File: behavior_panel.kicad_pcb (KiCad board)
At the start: 2 copper layers, 22 x 60 mm, 32 parts, among them J1 Conn_01x16, Q1 Q_NPN_BEC, Q3 N-channel MOSFET, U1 LM2902, U2 LM317_3PinPackage, U3 SFH617A-1X007T

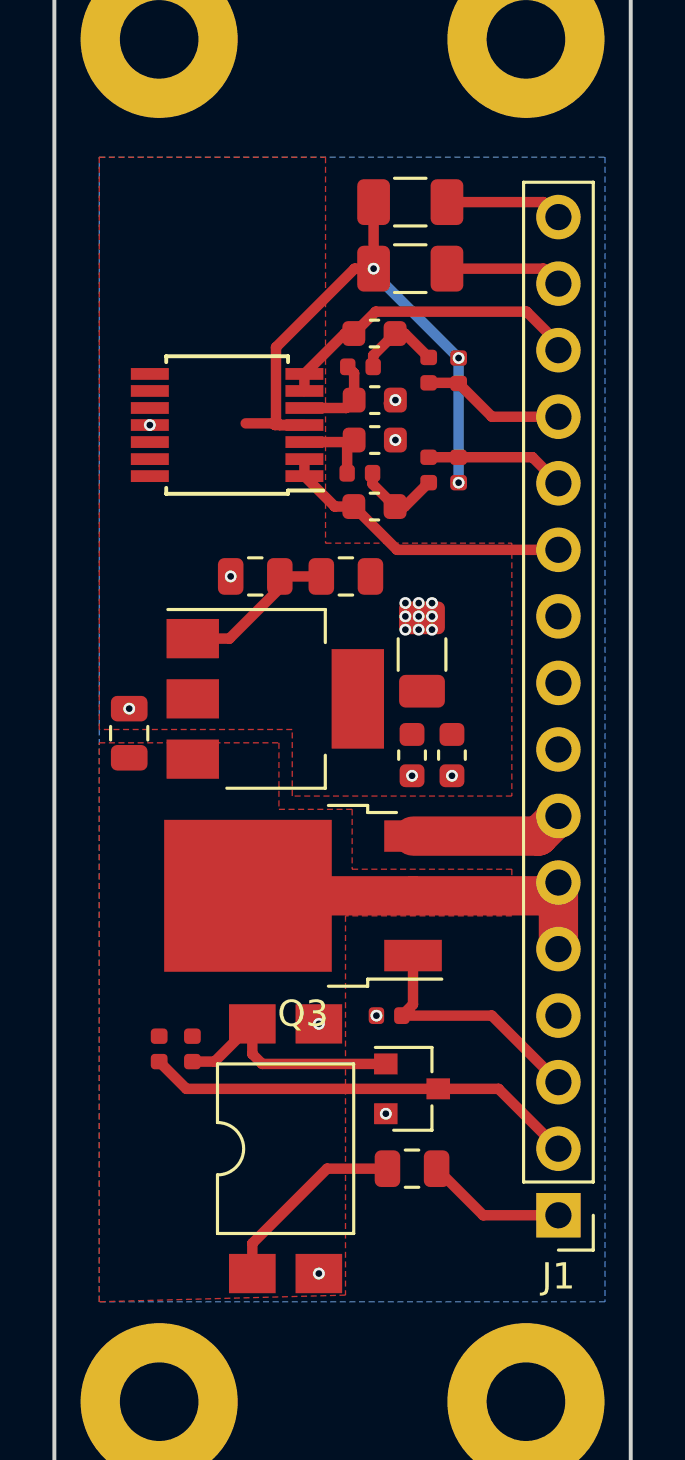
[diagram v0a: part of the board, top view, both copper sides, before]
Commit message: Fix bug in MOSFET light control
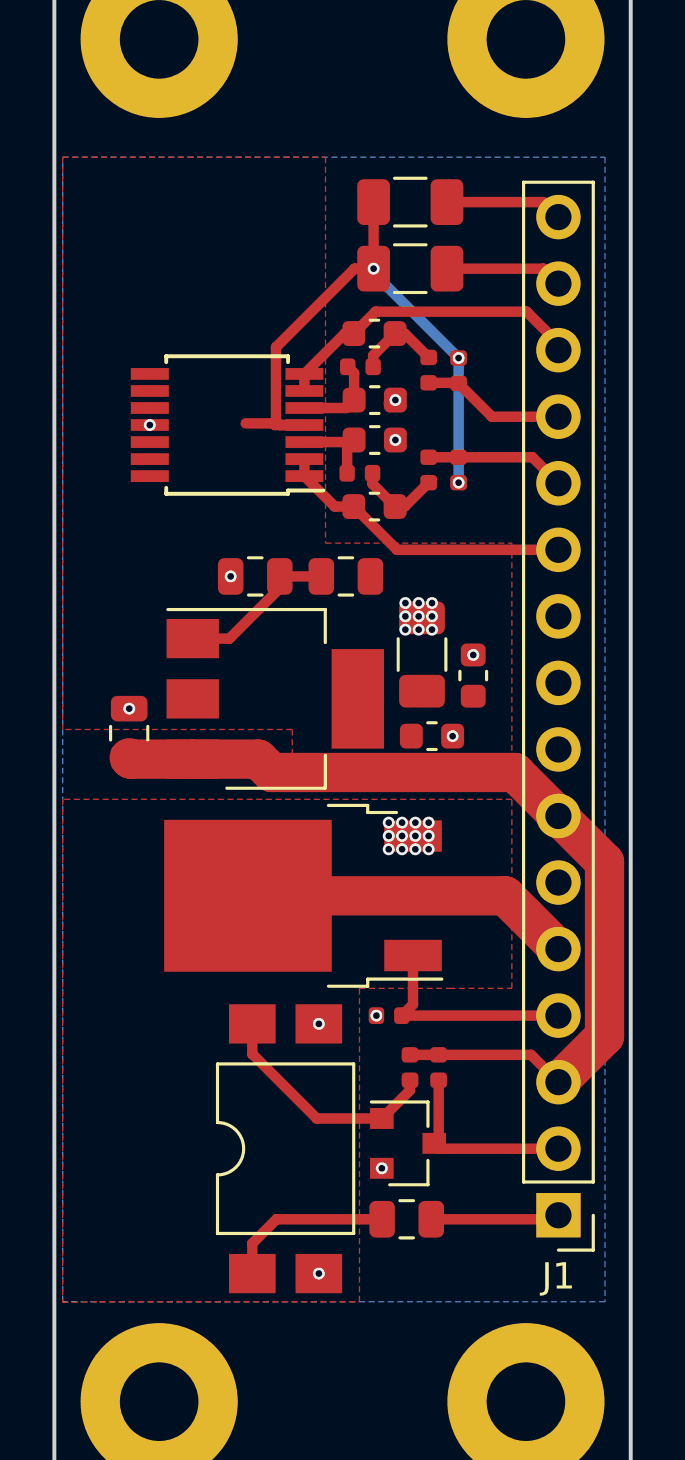
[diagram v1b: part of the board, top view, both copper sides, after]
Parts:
- moved R9 10.7 mm to (137.7, 82.2)
- moved R19 8.34 mm to (136.6, 82.2)
- moved C12 3.14 mm to (139.0, 67.3), turned to 90 degrees
- moved Q1 2.09 mm to (136.5, 85.1)
- moved R10 1.94 mm to (136.4, 88.0)
- moved C6 1.05 mm to (137.4, 69.6), turned to 180 degrees
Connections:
- net PD_IN renamed PD_CTL
- J1 pad 3: LT_IN -> +28V
- J1 pad 4: GND -> LT_CTL
- J1 pad 5: +28V -> LT_IN
- J1 pad 6: +28V -> GND
- J1 pad 7: LT_OUT -> +28V
- Q3 pad 1: LT_IN -> LT_CTL
- Q3 pad 2: +28V -> LT_IN
- Q3 pad 3: LT_OUT -> GND
- R25 pad 1: LT_IN -> LT_CTL
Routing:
- net +28V: track 14.6 -> 35.0 mm
- net PD_OUT: track 16.6 -> 7.30 mm
- net LT_CTL: track 0.00 -> 8.45 mm
- net LT_OUT: track 5.87 -> 0.00 mm
- net LT_IN: track 9.50 -> 12.7 mm
- net Net-(R10-Pad2): track 7.49 -> 6.49 mm
- net GND: vias 20 -> 32
- added copper zone on F.Cu, net LT_IN
- removed copper zone on F.Cu, net +28V
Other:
- board text added: "FROM LT"
- board text removed: "TO LT"

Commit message: Update to Kicad 6
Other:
- net class Default removed
- rule pad_to_mask_clearance: 0.2 -> 0

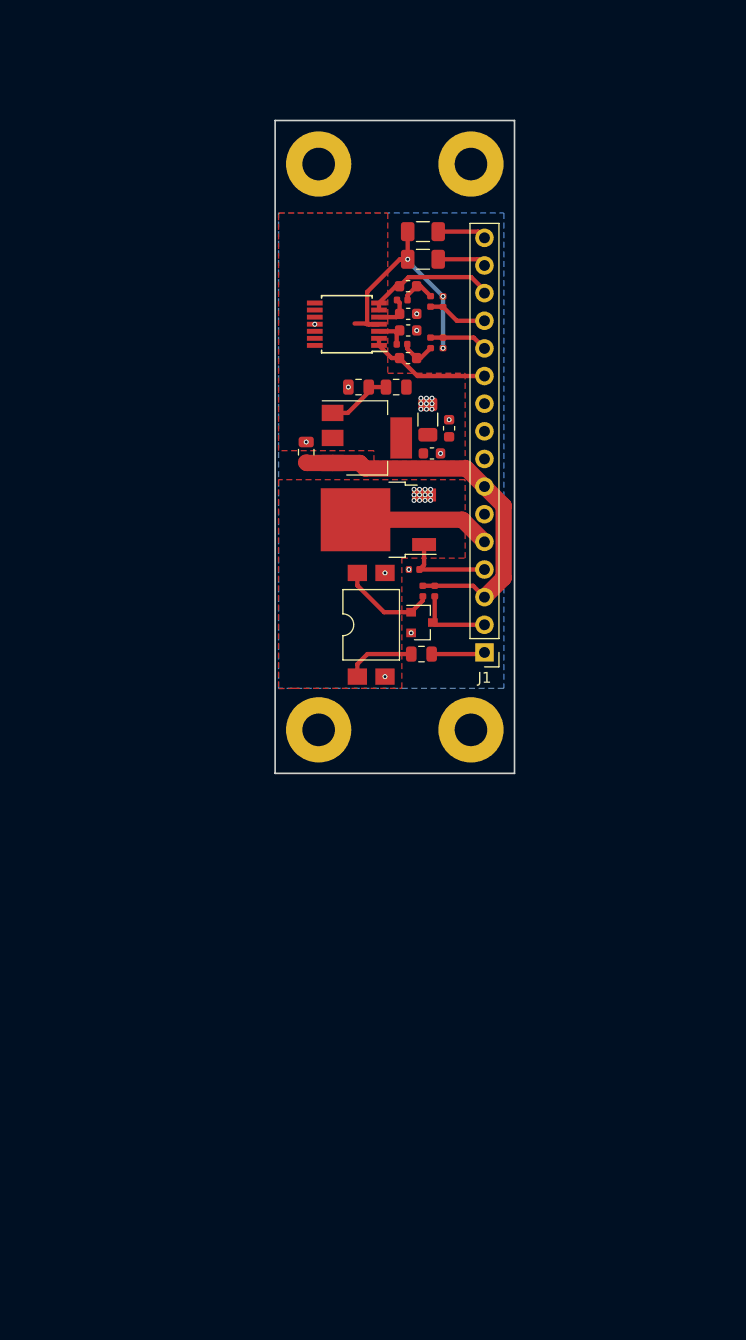
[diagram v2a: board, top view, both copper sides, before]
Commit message: Updated to include four power relays and four IR circuts
Went back to the through-hole, hand-solderable version.
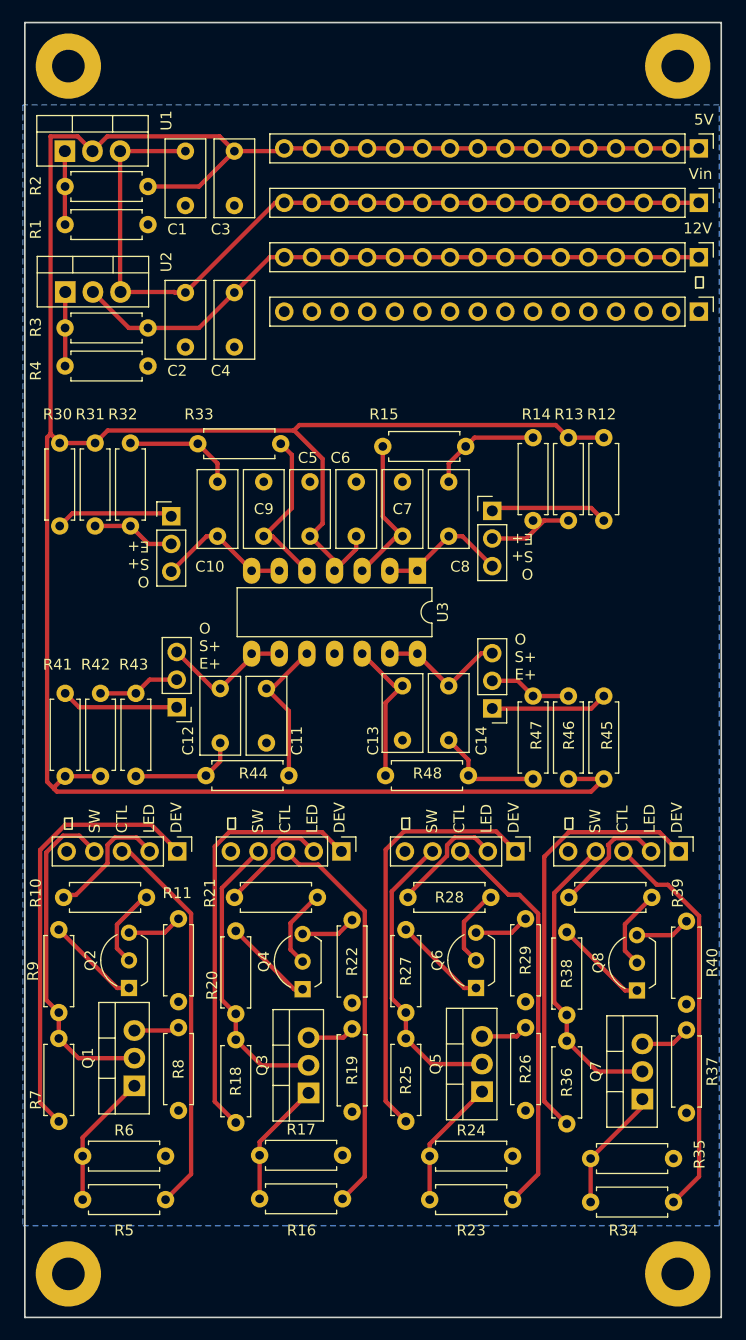
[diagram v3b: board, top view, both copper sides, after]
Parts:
- added C10: 0.1uF, Capacitor_THT:C_Rect_L7.0mm_W3.5mm_P5.00mm, F.Cu at (117.7, 77.2)
- added C13: 0.1uF, Capacitor_THT:C_Rect_L7.0mm_W3.5mm_P5.00mm, F.Cu at (134.7, 91.0)
- added C14: 0.1uF, Capacitor_THT:C_Rect_L7.0mm_W3.5mm_P5.00mm, F.Cu at (139.0, 91.0)
- added C7: 0.1uF, Capacitor_THT:C_Rect_L7.0mm_W3.5mm_P5.00mm, F.Cu at (134.7, 77.2)
- added C8: 0.1uF, Capacitor_THT:C_Rect_L7.0mm_W3.5mm_P5.00mm, F.Cu at (139.0, 77.2)
- added C9: 0.1uF, Capacitor_THT:C_Rect_L7.0mm_W3.5mm_P5.00mm, F.Cu at (122.0, 77.2)
- added J17: Conn_01x05_Pin, Connector_PinHeader_2.54mm:PinHeader_1x05_P2.54mm_Vertical, F.Cu at (114.0, 106.2)
- added J18: Conn_01x03_Pin, Connector_PinHeader_2.54mm:PinHeader_1x03_P2.54mm_Vertical, F.Cu at (143.0, 74.9)
- added J19: Conn_01x05_Pin, Connector_PinHeader_2.54mm:PinHeader_1x05_P2.54mm_Vertical, F.Cu at (129.1, 106.2)
- added J2: Conn_01x16, Connector_PinHeader_2.54mm:PinHeader_1x16_P2.54mm_Vertical, F.Cu at (161.9, 51.6)
- added J20: Conn_01x05_Pin, Connector_PinHeader_2.54mm:PinHeader_1x05_P2.54mm_Vertical, F.Cu at (145.1, 106.2)
- added J21: Conn_01x03_Pin, Connector_PinHeader_2.54mm:PinHeader_1x03_P2.54mm_Vertical, F.Cu at (113.5, 75.4)
- added J22: Conn_01x05_Pin, Connector_PinHeader_2.54mm:PinHeader_1x05_P2.54mm_Vertical, F.Cu at (160.1, 106.2)
- added J23: Conn_01x03_Pin, Connector_PinHeader_2.54mm:PinHeader_1x03_P2.54mm_Vertical, F.Cu at (114.0, 92.9)
- added J24: Conn_01x03_Pin, Connector_PinHeader_2.54mm:PinHeader_1x03_P2.54mm_Vertical, F.Cu at (143.0, 93.0)
- added J3: Conn_01x16, Connector_PinHeader_2.54mm:PinHeader_1x16_P2.54mm_Vertical, F.Cu at (161.9, 46.6)
- added J4: Conn_01x16, Connector_PinHeader_2.54mm:PinHeader_1x16_P2.54mm_Vertical, F.Cu at (161.9, 56.6)
- added Q2: Q_NPN_BCE, Package_TO_SOT_THT:TO-92L_Inline_Wide, F.Cu at (109.6, 118.7)
- added Q4: Q_NPN_BCE, Package_TO_SOT_THT:TO-92L_Inline_Wide, F.Cu at (125.5, 118.8)
- added Q5: N MOSFET, Package_TO_SOT_THT:TO-220-3_Vertical, F.Cu at (142.0, 128.3)
- added Q6: Q_NPN_BCE, Package_TO_SOT_THT:TO-92L_Inline_Wide, F.Cu at (141.5, 118.7)
- added Q7: N MOSFET, Package_TO_SOT_THT:TO-220-3_Vertical, F.Cu at (156.8, 128.9)
- added Q8: Q_NPN_BCE, Package_TO_SOT_THT:TO-92L_Inline_Wide, F.Cu at (156.3, 119.0)
- added R11: 10k, Resistor_THT:R_Axial_DIN0207_L6.3mm_D2.5mm_P7.62mm_Horizontal, F.Cu at (114.1, 112.4)
- added R12: 100 0.25W, Resistor_THT:R_Axial_DIN0207_L6.3mm_D2.5mm_P7.62mm_Horizontal, F.Cu at (153.2, 68.1)
- added R13: 10k, Resistor_THT:R_Axial_DIN0207_L6.3mm_D2.5mm_P7.62mm_Horizontal, F.Cu at (150.0, 68.1)
- added R14: 10k, Resistor_THT:R_Axial_DIN0207_L6.3mm_D2.5mm_P7.62mm_Horizontal, F.Cu at (146.7, 68.1)
- added R15: 10k, Resistor_THT:R_Axial_DIN0207_L6.3mm_D2.5mm_P7.62mm_Horizontal, F.Cu at (132.9, 69.0)
- added R16: 2.2k, Resistor_THT:R_Axial_DIN0207_L6.3mm_D2.5mm_P7.62mm_Horizontal, F.Cu at (129.2, 138.1)
- added R20: 10k, Resistor_THT:R_Axial_DIN0207_L6.3mm_D2.5mm_P7.62mm_Horizontal, F.Cu at (119.4, 121.1)
- added R21: 10k, Resistor_THT:R_Axial_DIN0207_L6.3mm_D2.5mm_P7.62mm_Horizontal, F.Cu at (119.3, 110.4)
- added R22: 10k, Resistor_THT:R_Axial_DIN0207_L6.3mm_D2.5mm_P7.62mm_Horizontal, F.Cu at (130.1, 112.5)
- added R23: 2.2k, Resistor_THT:R_Axial_DIN0207_L6.3mm_D2.5mm_P7.62mm_Horizontal, F.Cu at (144.8, 138.2)
- added R24: 10k, Resistor_THT:R_Axial_DIN0207_L6.3mm_D2.5mm_P7.62mm_Horizontal, F.Cu at (137.2, 134.2)
- added R26: R, Resistor_THT:R_Axial_DIN0207_L6.3mm_D2.5mm_P7.62mm_Horizontal, F.Cu at (146.0, 122.4)
- added R27: 10k, Resistor_THT:R_Axial_DIN0207_L6.3mm_D2.5mm_P7.62mm_Horizontal, F.Cu at (135.0, 121.0)
- added R28: 10k, Resistor_THT:R_Axial_DIN0207_L6.3mm_D2.5mm_P7.62mm_Horizontal, F.Cu at (135.2, 110.4)
- added R29: 10k, Resistor_THT:R_Axial_DIN0207_L6.3mm_D2.5mm_P7.62mm_Horizontal, F.Cu at (146.0, 112.4)
- added R30: 100 0.25W, Resistor_THT:R_Axial_DIN0207_L6.3mm_D2.5mm_P7.62mm_Horizontal, F.Cu at (103.2, 68.6)
- added R31: 10k, Resistor_THT:R_Axial_DIN0207_L6.3mm_D2.5mm_P7.62mm_Horizontal, F.Cu at (106.5, 68.6)
- added R32: 10k, Resistor_THT:R_Axial_DIN0207_L6.3mm_D2.5mm_P7.62mm_Horizontal, F.Cu at (109.7, 68.6)
- added R33: 10k, Resistor_THT:R_Axial_DIN0207_L6.3mm_D2.5mm_P7.62mm_Horizontal, F.Cu at (123.5, 68.7)
- added R34: 2.2k, Resistor_THT:R_Axial_DIN0207_L6.3mm_D2.5mm_P7.62mm_Horizontal, F.Cu at (159.6, 138.4)
- added R35: 10k, Resistor_THT:R_Axial_DIN0207_L6.3mm_D2.5mm_P7.62mm_Horizontal, F.Cu at (152.0, 134.4)
- added R36: 50, Resistor_THT:R_Axial_DIN0207_L6.3mm_D2.5mm_P7.62mm_Horizontal, F.Cu at (149.8, 123.6)
- added R37: R, Resistor_THT:R_Axial_DIN0207_L6.3mm_D2.5mm_P7.62mm_Horizontal, F.Cu at (160.8, 122.6)
- added R38: 10k, Resistor_THT:R_Axial_DIN0207_L6.3mm_D2.5mm_P7.62mm_Horizontal, F.Cu at (149.8, 121.2)
- added R39: 10k, Resistor_THT:R_Axial_DIN0207_L6.3mm_D2.5mm_P7.62mm_Horizontal, F.Cu at (150.0, 110.4)
- added R40: 10k, Resistor_THT:R_Axial_DIN0207_L6.3mm_D2.5mm_P7.62mm_Horizontal, F.Cu at (160.8, 112.6)
- added R41: 100 0.25W, Resistor_THT:R_Axial_DIN0207_L6.3mm_D2.5mm_P7.62mm_Horizontal, F.Cu at (103.7, 99.3)
- added R42: 10k, Resistor_THT:R_Axial_DIN0207_L6.3mm_D2.5mm_P7.62mm_Horizontal, F.Cu at (107.0, 99.3)
- added R43: 10k, Resistor_THT:R_Axial_DIN0207_L6.3mm_D2.5mm_P7.62mm_Horizontal, F.Cu at (110.2, 99.3)
- added R44: 10k, Resistor_THT:R_Axial_DIN0207_L6.3mm_D2.5mm_P7.62mm_Horizontal, F.Cu at (124.3, 99.2)
- added R45: 100 0.25W, Resistor_THT:R_Axial_DIN0207_L6.3mm_D2.5mm_P7.62mm_Horizontal, F.Cu at (153.2, 99.5)
- added R46: 10k, Resistor_THT:R_Axial_DIN0207_L6.3mm_D2.5mm_P7.62mm_Horizontal, F.Cu at (150.0, 99.5)
- added R47: 10k, Resistor_THT:R_Axial_DIN0207_L6.3mm_D2.5mm_P7.62mm_Horizontal, F.Cu at (146.7, 99.5)
- added R48: 10k, Resistor_THT:R_Axial_DIN0207_L6.3mm_D2.5mm_P7.62mm_Horizontal, F.Cu at (133.1, 99.2)
- C1, C2, C6: footprint Capacitor_SMD:C_0603_1608Metric -> Capacitor_THT:C_Rect_L7.0mm_W3.5mm_P5.00mm
- C11: footprint Capacitor_SMD:C_0805_2012Metric -> Capacitor_THT:C_Rect_L7.0mm_W3.5mm_P5.00mm
- C12: value 1uF -> 0.1uF; footprint Capacitor_SMD:C_0603_1608Metric -> Capacitor_THT:C_Rect_L7.0mm_W3.5mm_P5.00mm
- C3, C4: value 0.1uF -> 1uF; footprint Capacitor_SMD:C_0603_1608Metric -> Capacitor_THT:C_Rect_L7.0mm_W3.5mm_P5.00mm
- C5: footprint Capacitor_SMD:C_1206_3216Metric -> Capacitor_THT:C_Rect_L7.0mm_W3.5mm_P5.00mm
- Q1: value Q_NPN_BEC -> N MOSFET; footprint Package_TO_SOT_SMD:SOT-23 -> Package_TO_SOT_THT:TO-220-3_Vertical
- Q3: value N-channel MOSFET -> N MOSFET; footprint Package_TO_SOT_SMD:TO-252-2 -> Package_TO_SOT_THT:TO-220-3_Vertical
- R1: value 100 0.25W -> 100; footprint Resistor_SMD:R_1206_3216Metric -> Resistor_THT:R_Axial_DIN0207_L6.3mm_D2.5mm_P7.62mm_Horizontal
- R10: value 220 -> 10k; footprint Resistor_SMD:R_0805_2012Metric -> Resistor_THT:R_Axial_DIN0207_L6.3mm_D2.5mm_P7.62mm_Horizontal
- R17: value 100 -> 10k; footprint Resistor_SMD:R_0805_2012Metric -> Resistor_THT:R_Axial_DIN0207_L6.3mm_D2.5mm_P7.62mm_Horizontal
- R18: value 300 -> 50; footprint Resistor_SMD:R_0805_2012Metric -> Resistor_THT:R_Axial_DIN0207_L6.3mm_D2.5mm_P7.62mm_Horizontal
- R19, R8: value 10k -> R; footprint Resistor_SMD:R_0402_1005Metric -> Resistor_THT:R_Axial_DIN0207_L6.3mm_D2.5mm_P7.62mm_Horizontal
- R2: value 100 0.25W -> 300; footprint Resistor_SMD:R_1206_3216Metric -> Resistor_THT:R_Axial_DIN0207_L6.3mm_D2.5mm_P7.62mm_Horizontal
- R25, R7: value 10k -> 50; footprint Resistor_SMD:R_0402_1005Metric -> Resistor_THT:R_Axial_DIN0207_L6.3mm_D2.5mm_P7.62mm_Horizontal
- R3: value 10k -> 100; footprint Resistor_SMD:R_0402_1005Metric -> Resistor_THT:R_Axial_DIN0207_L6.3mm_D2.5mm_P7.62mm_Horizontal
- R4: value 10k -> 860; footprint Resistor_SMD:R_0402_1005Metric -> Resistor_THT:R_Axial_DIN0207_L6.3mm_D2.5mm_P7.62mm_Horizontal
- R5: value 10k -> 2.2k; footprint Resistor_SMD:R_0402_1005Metric -> Resistor_THT:R_Axial_DIN0207_L6.3mm_D2.5mm_P7.62mm_Horizontal
- R6, R9: footprint Resistor_SMD:R_0402_1005Metric -> Resistor_THT:R_Axial_DIN0207_L6.3mm_D2.5mm_P7.62mm_Horizontal
- U1: value LM2902 -> LM317_3PinPackage; footprint Package_SO:TSSOP-14_4.4x5mm_P0.65mm -> Package_TO_SOT_THT:TO-220-3_Vertical
- U2: footprint Package_TO_SOT_SMD:SOT-223 -> Package_TO_SOT_THT:TO-220-3_Vertical
- U3: value SFH617A-1X007T -> LM2902; footprint Package_DIP:SMDIP-4_W9.53mm_Clearance8mm -> Package_DIP:DIP-14_W7.62mm_LongPads
- moved H2 108.5 mm to (104.0, 145.0)
- moved H1 107.2 mm to (160.0, 145.0)
- moved R6 84.8 mm to (105.3, 134.2), turned to 0 degrees
- moved R5 82.4 mm to (112.9, 138.2), turned to 180 degrees
- moved R17 71.7 mm to (121.6, 134.1), turned to 0 degrees
- moved H4 71.3 mm to (104.0, 34.0)
- moved R7 71.2 mm to (103.1, 123.4), turned to -90 degrees
- moved R8 70.0 mm to (114.1, 122.4), turned to -90 degrees
- moved H3 69.4 mm to (160.0, 34.0)
- moved R18 61.0 mm to (119.4, 123.5), turned to -90 degrees
- moved Q3 53.1 mm to (126.1, 128.4), turned to 90 degrees
- moved R9 51.9 mm to (103.1, 121.0)
- moved J1 50.3 mm to (161.9, 41.6), turned to -90 degrees
- moved Q1 50.1 mm to (110.1, 127.7), turned to 90 degrees
- moved R25 43.1 mm to (135.0, 123.4), turned to -90 degrees
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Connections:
- C1 pad 1: Net-(C1-Pad1) -> VIN
- C11 pad 1: +28V -> Net-(U3C-+)
- C12 pad 1: 5V -> /IR circuit2/O
- C12 pad 2: GND -> Net-(C12-Pad2)
- C2 pad 1: Net-(C2-Pad1) -> VIN
- C3 pad 1: O1 -> 5V
- C3 pad 2: Net-(C3-Pad2) -> GND
- C4 pad 1: O2 -> 12V
- C4 pad 2: Net-(C4-Pad2) -> GND
- H1 pad 1: (no net) -> unconnected-(H1-Pin_1-Pad1)
- H2 pad 1: (no net) -> unconnected-(H2-Pin_1-Pad1)
- H3 pad 1: (no net) -> unconnected-(H3-Pin_1-Pad1)
- H4 pad 1: (no net) -> unconnected-(H4-Pin_1-Pad1)
- J1 pad 1: PD_CTL -> 5V
- J1 pad 10: GND -> 5V
- J1 pad 11: O1 -> 5V
- J1 pad 12: S1+ -> 5V
- J1 pad 13: S2+ -> 5V
- J1 pad 14: O2 -> 5V
- J1 pad 15: E1+ -> 5V
- J1 pad 16: E2+ -> 5V
- J1 pad 2: PD_OUT -> 5V
- J1 pad 3: +28V -> 5V
- J1 pad 4: LT_CTL -> 5V
- J1 pad 5: LT_IN -> 5V
- J1 pad 6: GND -> 5V
- J1 pad 7: +28V -> 5V
- J1 pad 8: GND -> 5V
- J1 pad 9: GND -> 5V
- Q1 pad 1: Net-(Q1-Pad1) -> Net-(Q1-G)
- Q1 pad 2: GND -> /power control/switch out
- Q1 pad 3: PD_OUT -> Net-(Q1-S)
- Q3 pad 1: LT_CTL -> Net-(Q3-G)
- Q3 pad 2: LT_IN -> /power control2/switch out
- Q3 pad 3: GND -> Net-(Q3-S)
- R1 pad 2: E1+ -> Net-(U1-ADJ)
- R10 pad 1: PD_CTL -> /power control/LED in
- R10 pad 2: Net-(R10-Pad2) -> Net-(Q2-C)
- R17 pad 1: 5V -> Net-(Q3-G)
- R17 pad 2: Net-(R17-Pad2) -> GND
- R18 pad 1: Net-(R17-Pad2) -> /power control2/switch out
- R18 pad 2: GND -> /power control2/device in
- R19 pad 1: Net-(Q1-Pad1) -> Net-(Q3-S)
- R19 pad 2: +28V -> GND
- R2 pad 1: 5V -> Net-(U1-ADJ)
- R2 pad 2: E2+ -> GND
- R25 pad 1: LT_CTL -> /power control3/switch out
- R25 pad 2: GND -> /power control3/device in
- R3 pad 1: 5V -> 12V
- R3 pad 2: S1+ -> Net-(U2-ADJ)
- R4 pad 1: 5V -> Net-(U2-ADJ)
- R4 pad 2: S2+ -> GND
- R5 pad 1: Net-(C3-Pad2) -> /power control/CTL
- R5 pad 2: S1+ -> Net-(Q1-G)
- R6 pad 1: Net-(C4-Pad2) -> Net-(Q1-G)
- R6 pad 2: S2+ -> GND
- R7 pad 1: Net-(C1-Pad1) -> /power control/switch out
- R7 pad 2: Net-(C3-Pad2) -> /power control/device in
- R8 pad 1: Net-(C2-Pad1) -> Net-(Q1-S)
- R8 pad 2: Net-(C4-Pad2) -> GND
- R9 pad 1: PD_OUT -> /power control/switch out
- R9 pad 2: +28V -> Net-(Q2-B)
- U1 pad 1: O1 -> Net-(U1-ADJ)
- U1 pad 2: O1 -> 5V
- U1 pad 3: Net-(C1-Pad1) -> VIN
- U2 pad 1: Net-(R17-Pad2) -> Net-(U2-ADJ)
- U2 pad 2: 5V -> 12V
- U2 pad 3: +28V -> VIN
- U3 pad 1: Net-(R10-Pad2) -> /IR circuit1/O
- U3 pad 2: GND -> /IR circuit1/O
- U3 pad 3: GND -> Net-(U3A-+)
- U3 pad 4: Net-(Q1-Pad1) -> 5V
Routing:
- net 5V: track 23.3 -> 262.0 mm, vias 3 -> 0
- net VIN: track 0.00 -> 75.5 mm
- net 12V: track 0.00 -> 59.7 mm
- net /power control/device in: track 0.00 -> 40.2 mm
- net /power control4/device in: track 0.00 -> 39.4 mm
- net /power control3/device in: track 0.00 -> 39.1 mm
- net /power control2/device in: track 0.00 -> 39.1 mm
- net /power control3/CTL: track 0.00 -> 36.8 mm
- net /power control2/CTL: track 0.00 -> 36.8 mm
- net /power control4/CTL: track 0.00 -> 36.7 mm
- net /power control/CTL: track 0.00 -> 36.0 mm
- net +28V: track 35.0 -> 0.00 mm
- net /power control/switch out: track 0.00 -> 30.9 mm
- net /power control4/switch out: track 0.00 -> 27.6 mm
- net /power control3/switch out: track 0.00 -> 27.3 mm
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- removed copper zone on F.Cu, net 5V
- removed copper zone on F.Cu, net LT_IN
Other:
- board size 22 x 60 mm -> 64 x 119 mm
- rule pad_to_mask_clearance: 0 -> 0.0508
- board text added: "12V"
- board text added: "5V"
- board text added: "CTL"
- board text added: "DEV"
- board text added: "LBHB master behavior circuit (4/16/2024) Designed by Brad Buran & Satya Parida"
- board text added: "LED"
- board text added: "O S+ E+"
- board text added: "SW"
- board text added: "Vin"
- board text added: "⏚"
- board text removed: "28V"
- board text removed: "E1"
- board text removed: "E2"
- board text removed: "FROM LT"
- board text removed: "G"
- board text removed: "LT CTL (NI)"
- board text removed: "O1"
- board text removed: "O2"
- board text removed: "PD CTL (NI)"
- board text removed: "S1"
- board text removed: "S2"
- board text removed: "TO PD"

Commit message: Update connectors to be smaller
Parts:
- removed J4: Conn_01x16, Connector_PinHeader_2.54mm:PinHeader_1x16_P2.54mm_Vertical
- removed R18, R25, R36, R7: 50, Resistor_THT:R_Axial_DIN0207_L6.3mm_D2.5mm_P7.62mm_Horizontal
- added J5: Conn_01x04, Connector_PinHeader_2.54mm:PinHeader_1x04_P2.54mm_Vertical, F.Cu at (131.3, 56.7)
- J1, J2, J3: value Conn_01x16 -> Conn_01x04; footprint Connector_PinHeader_2.54mm:PinHeader_1x16_P2.54mm_Vertical -> Connector_PinHeader_2.54mm:PinHeader_1x04_P2.54mm_Vertical
- R19, R26, R37, R8: value R -> 50
- moved J1 30.4 mm to (131.5, 41.6)
- moved J2 30.4 mm to (131.5, 51.6)
- moved J3 30.3 mm to (131.6, 46.5)
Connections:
- J17 pad 4: /power control/switch out -> /power control/device in
- J19 pad 4: /power control2/switch out -> /power control2/device in
- J20 pad 4: /power control3/switch out -> /power control3/device in
- J22 pad 4: /power control4/switch out -> /power control4/device in
- Q1 pad 2: /power control/switch out -> /power control/device in
- Q3 pad 2: /power control2/switch out -> /power control2/device in
- Q5 pad 2: /power control3/switch out -> /power control3/device in
- Q7 pad 2: /power control4/switch out -> /power control4/device in
- R20 pad 1: /power control2/switch out -> /power control2/device in
- R27 pad 1: /power control3/switch out -> /power control3/device in
- R38 pad 1: /power control4/switch out -> /power control4/device in
- R9 pad 1: /power control/switch out -> /power control/device in
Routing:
- net /power control/device in: track 40.2 -> 71.1 mm
- net /power control/switch out: track 30.9 -> 0.00 mm
- net /power control4/switch out: track 27.6 -> 0.00 mm
- net /power control4/device in: track 39.4 -> 67.0 mm
- net /power control3/switch out: track 27.3 -> 0.00 mm
- net /power control3/device in: track 39.1 -> 66.4 mm
- net /power control2/device in: track 39.1 -> 66.0 mm
- net /power control2/switch out: track 26.9 -> 0.00 mm
